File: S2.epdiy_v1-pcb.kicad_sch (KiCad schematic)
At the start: 93 parts, among them J1 USB_C_Receptacle_USB2.0, J2 Jack-DC, P1 CONN_02X13, Q1 MMBT3904, Q2 MMBT3904, SW1 RESET, SW2 BOOT, U1 MCP1700-3302E_SOT23, U11 TP4056, U2 ESP32-S2-WROVER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

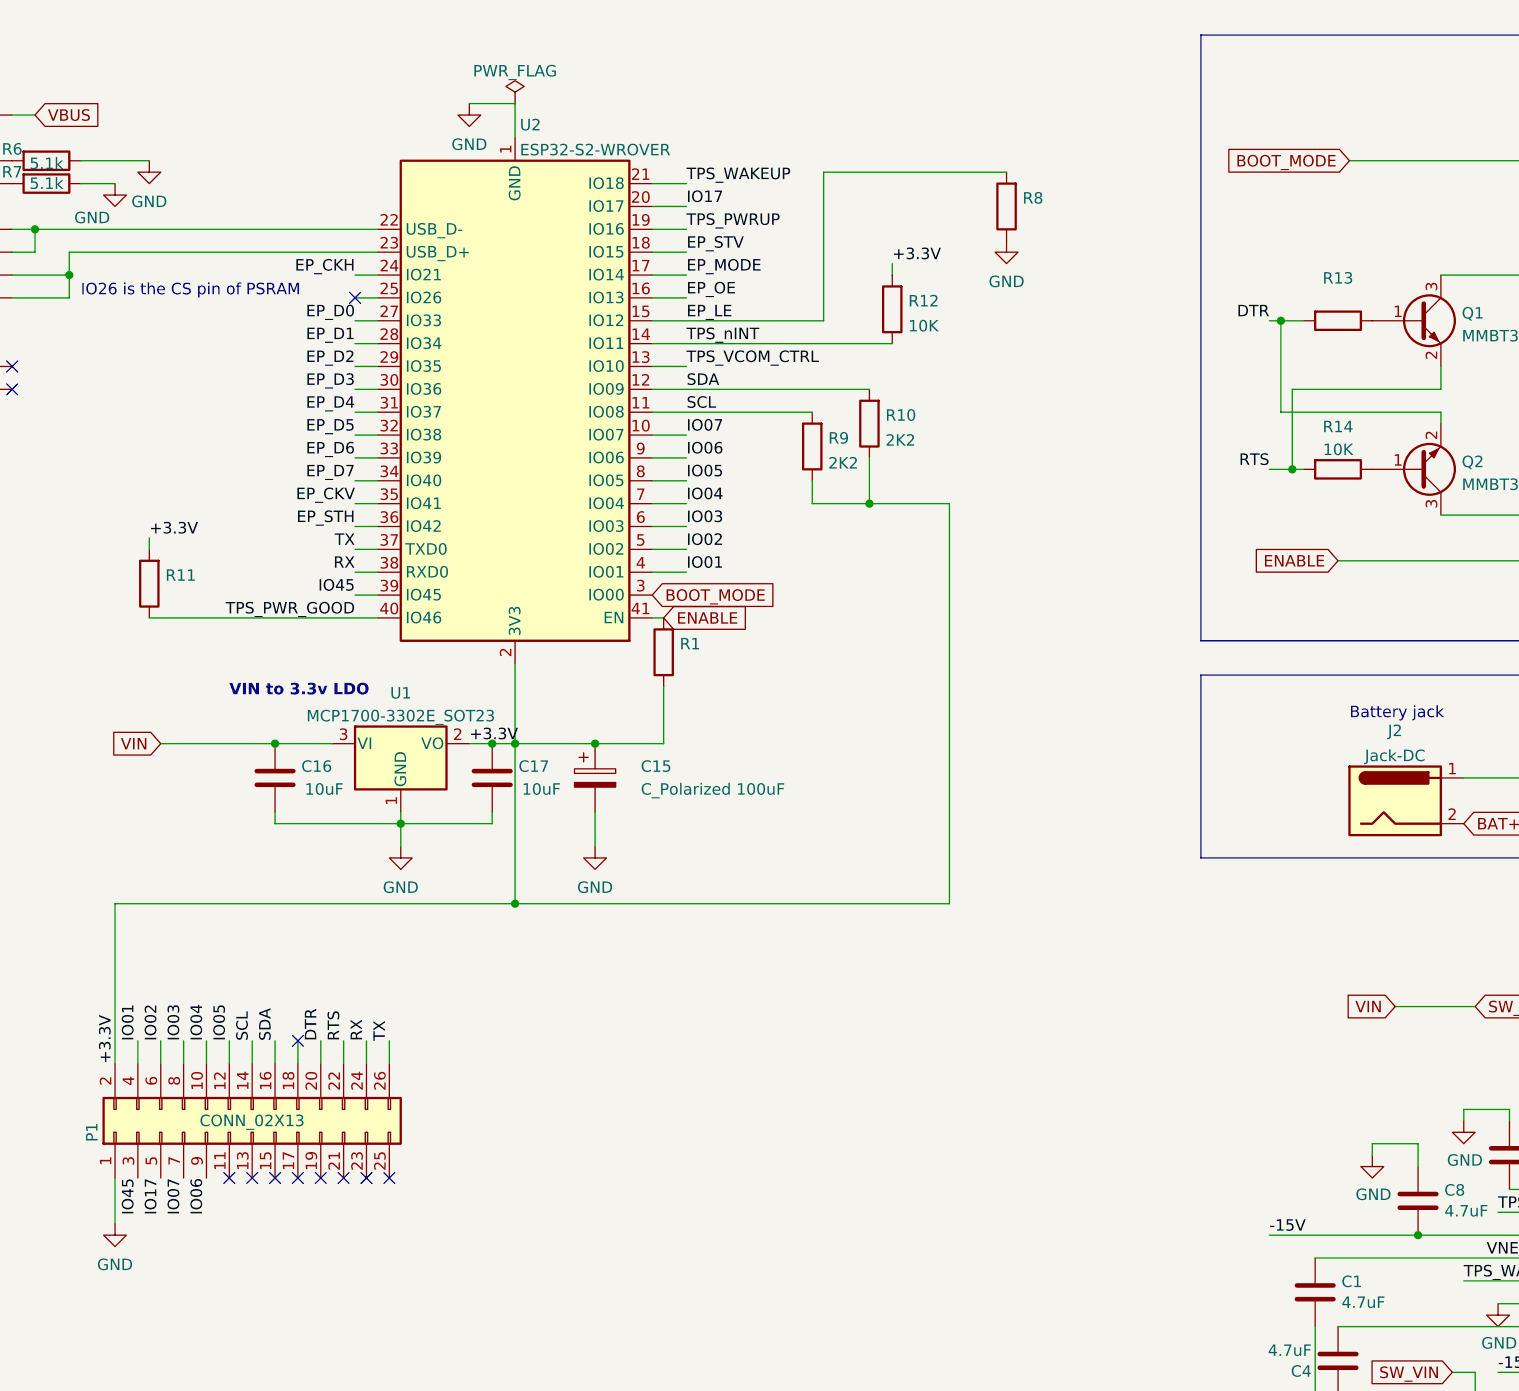
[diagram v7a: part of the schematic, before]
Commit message: Modify IO config and use Realtime ones for I2S
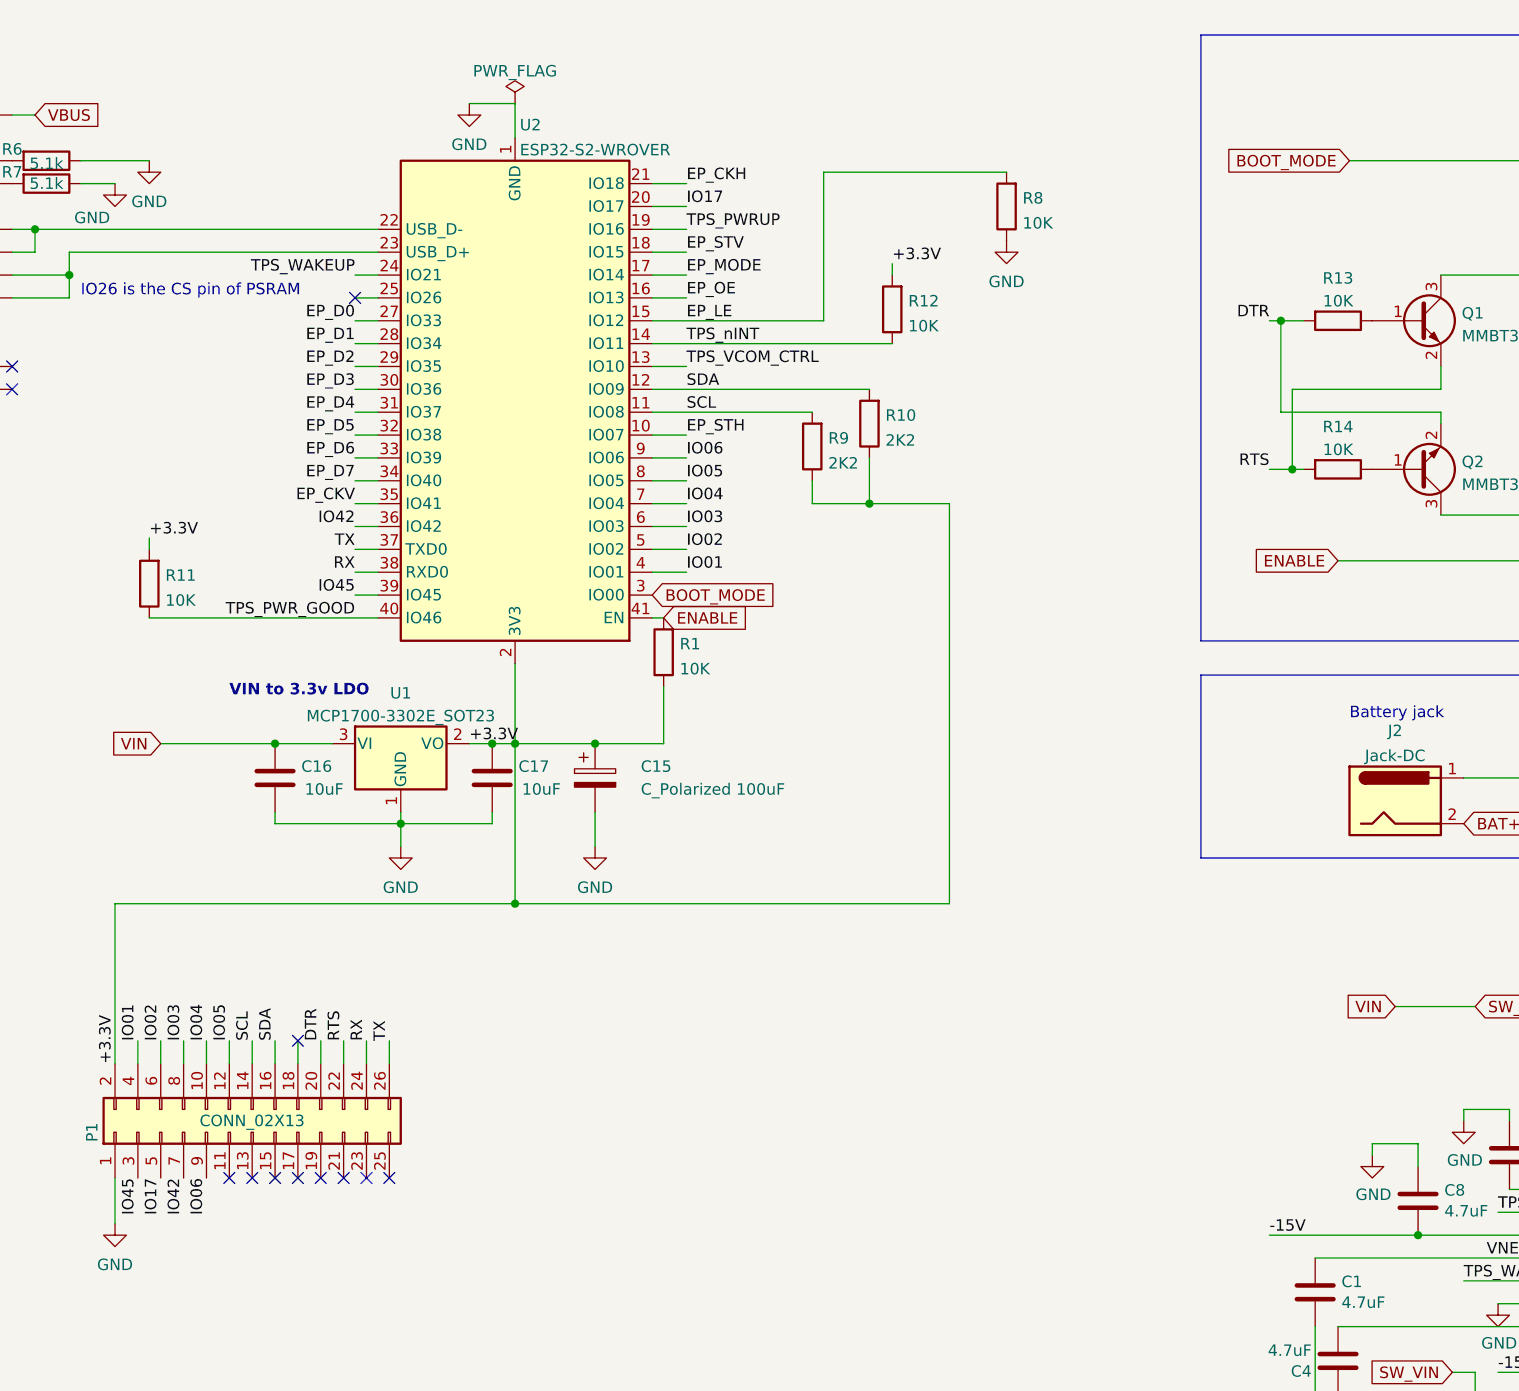
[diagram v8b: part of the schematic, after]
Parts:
- R1, R11, R13, R8: value (none) -> 10K; footprint (none) -> Resistor_SMD:R_0603_1608Metric
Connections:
- net EP_CKH: now also U2.21 (IO18); no longer U2.24 (IO21)
- net EP_STH: now also U2.10 (IO07); no longer U2.36 (IO42)
- net TPS_WAKEUP: now also U2.24 (IO21); no longer U2.21 (IO18)
- net IO07 renamed IO42
- net IO42: now also U2.36 (IO42); no longer U2.10 (IO07)
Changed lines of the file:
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@@
     (effects (font (size 1.27 1.27)) (justify left bottom))
   )
-  (label "IO07" (at 95.25 153.67 270)
+  (label "IO42" (at 95.25 153.67 270)
     (effects (font (size 1.27 1.27)) (justify right bottom))
   )
@@
     (effects (font (size 1.27 1.27)) (justify left bottom))
   )
+  (label "IO42" (at 114.3 81.28 180)
+    (effects (font (size 1.27 1.27)) (justify right bottom))
+  )
   (label "IO17" (at 151.13 45.72 0)
     (effects (font (size 1.27 1.27)) (justify left bottom))
@@
     (effects (font (size 1.27 1.27)) (justify left bottom))
   )
-  (label "TPS_WAKEUP" (at 151.13 43.18 0)
+  (label "EP_STH" (at 151.13 71.12 0)
     (effects (font (size 1.27 1.27)) (justify left bottom))
   )
@@
     (effects (font (size 1.27 1.27)) (justify left bottom))
   )
-  (label "EP_CKH" (at 114.3 53.34 180)
-    (effects (font (size 1.27 1.27)) (justify right bottom))
-  )
   (label "TPS_WAKEUP" (at 237.49 165.1 0)
     (effects (font (size 1.27 1.27)) (justify left bottom))
@@
     (effects (font (size 1.27 1.27)) (justify right bottom))
   )
-  (label "IO07" (at 151.13 71.12 0)
-    (effects (font (size 1.27 1.27)) (justify left bottom))
-  )
   (label "TPS_nINT" (at 241.3 157.48 0)
     (effects (font (size 1.27 1.27)) (justify left bottom))
@@
     (effects (font (size 1.27 1.27)) (justify left bottom))
   )
-  (label "EP_STH" (at 114.3 81.28 180)
-    (effects (font (size 1.27 1.27)) (justify right bottom))
-  )
   (label "EP_MODE" (at 57.15 255.27 0)
     (effects (font (size 1.27 1.27)) (justify left bottom))
@@
     (effects (font (size 1.27 1.27)) (justify left bottom))
   )
+  (label "TPS_WAKEUP" (at 114.3 53.34 180)
+    (effects (font (size 1.27 1.27)) (justify right bottom))
+  )
   (label "15V" (at 243.84 200.66 0)
     (effects (font (size 1.27 1.27)) (justify left bottom))
@@
   )
   (label "EP_CKH" (at 57.15 207.01 0)
+    (effects (font (size 1.27 1.27)) (justify left bottom))
+  )
+  (label "EP_CKH" (at 151.13 43.18 0)
     (effects (font (size 1.27 1.27)) (justify left bottom))
   )
@@
     (in_bom yes) (on_board yes) (fields_autoplaced)
     (property "Reference" "R13" (id 0) (at 223.52 53.7042 90))
-    (property "Value" "" (id 1) (at 223.52 56.2411 90))
-    (property "Footprint" "" (id 2) (at 223.52 56.642 90)
+    (property "Value" "10K" (id 1) (at 223.52 56.2411 90))
+    (property "Footprint" "Resistor_SMD:R_0603_1608Metric" (id 2) (at 223.52 56.642 90)
       (effects (font (size 1.27 1.27)) hide)
     )
@@
       (effects (font (size 1.27 1.27)) (justify right))
     )
-    (property "Value" "" (id 1) (at 93.218 89.4966 0)
-      (effects (font (size 1.27 1.27)) (justify right))
-    )
-    (property "Footprint" "" (id 2) (at 93.218 87.63 90)
+    (property "Value" "10K" (id 1) (at 93.218 89.4966 0)
+      (effects (font (size 1.27 1.27)) (justify right))
+    )
+    (property "Footprint" "Resistor_SMD:R_0603_1608Metric" (id 2) (at 93.218 87.63 90)
       (effects (font (size 1.27 1.27)) hide)
     )
@@
       (effects (font (size 1.27 1.27)) (justify right))
     )
-    (property "Value" "" (id 1) (at 188.468 47.5866 0)
-      (effects (font (size 1.27 1.27)) (justify right))
-    )
-    (property "Footprint" "" (id 2) (at 188.468 45.72 90)
+    (property "Value" "10K" (id 1) (at 188.468 47.5866 0)
+      (effects (font (size 1.27 1.27)) (justify right))
+    )
+    (property "Footprint" "Resistor_SMD:R_0603_1608Metric" (id 2) (at 188.468 45.72 90)
       (effects (font (size 1.27 1.27)) hide)
     )
@@
       (effects (font (size 1.27 1.27)) (justify right))
     )
-    (property "Value" "" (id 1) (at 150.368 97.1166 0)
-      (effects (font (size 1.27 1.27)) (justify right))
-    )
-    (property "Footprint" "" (id 2) (at 150.368 95.25 90)
-      (effects (font (size 1.27 1.27)) hide)
-    )
+    (property "Value" "10K" (id 1) (at 150.368 97.1166 0)
+      (effects (font (size 1.27 1.27)) (justify right))
+    )
+    (property "Footprint" "Resistor_SMD:R_0603_1608Metric" (id 2) (at 150.368 95.25 90)
+      (effects (font (size 1.27 1.27)) hide)
+    )
